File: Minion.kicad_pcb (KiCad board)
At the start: 0 parts

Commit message: finished most of pcb, added 3d models
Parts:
- added BT1: Battery, Connector_JST:JST_PH_S2B-PH-K_1x02_P2.00mm_Horizontal, F.Cu at (219.1, 155.0)
- added C1: 10uF, Capacitor_SMD:C_0805_2012Metric, F.Cu at (210.0, 157.0)
- added C10: 0.1uF, Capacitor_SMD:C_0805_2012Metric, F.Cu at (189.5, 122.5)
- added C11: 10uF, Capacitor_SMD:C_0805_2012Metric, F.Cu at (202.5, 153.5)
- added C2: 1uF, Capacitor_SMD:C_0805_2012Metric, F.Cu at (184.5, 124.5)
- added C3: 0.1uF, Capacitor_SMD:C_0805_2012Metric, F.Cu at (170.0, 135.5)
- added C4: 10uF, Capacitor_SMD:C_0805_2012Metric, F.Cu at (170.0, 139.0)
- added C5: 10uF, Capacitor_SMD:C_0805_2012Metric, F.Cu at (202.0, 125.5)
- added C6: 0.1uF, Capacitor_SMD:C_0805_2012Metric, F.Cu at (199.5, 125.5)
- added C7: 10uF, Capacitor_SMD:C_0805_2012Metric, F.Cu at (206.9, 115.0)
- added C8: 0.1uF, Capacitor_SMD:C_0805_2012Metric, F.Cu at (210.0, 118.0)
- added C9: 0.1uF, Capacitor_SMD:C_0805_2012Metric, F.Cu at (198.0, 101.5)
- added D1: PWRLED, LED_SMD:LED_0805_2012Metric, F.Cu at (210.5, 114.0)
- added D2: WS2812B, LED_SMD:LED_WS2812B_PLCC4_5.0x5.0mm_P3.2mm, B.Cu at (191.6, 135.3)
- added D3: WS2812B, LED_SMD:LED_WS2812B_PLCC4_5.0x5.0mm_P3.2mm, B.Cu at (201.1, 135.3)
- added D4: WS2812B, LED_SMD:LED_WS2812B_PLCC4_5.0x5.0mm_P3.2mm, B.Cu at (201.1, 127.5)
- added D5: WS2812B, LED_SMD:LED_WS2812B_PLCC4_5.0x5.0mm_P3.2mm, B.Cu at (191.5, 127.7)
- added D6: S-LMBR340FT1G, Diode_SMD:D_0805_2012Metric, F.Cu at (195.5, 108.0)
- added D8: Orange, LED_SMD:LED_0805_2012Metric, F.Cu at (212.0, 150.0)
- added D9: MBR0540, Diode_SMD:D_SOD-123, F.Cu at (206.5, 150.5)
- added DISPLAY_SSD1351: Conn_01x07_Socket, Connector_PinHeader_2.54mm:SSD_1351, F.Cu at (175.0, 123.3)
- added J1: USB_C_Receptacle_USB2.0_16P, Connector_USB:USB_C_Receptacle_HCTL_HC-TYPE-C-16P-01A, F.Cu at (204.5, 103.0)
- added J2: USB_A, Connector_USB:USB_A_Molex_105057_Vertical, F.Cu at (171.0, 156.5)
- added J3: Micro_SD_Card, Connector_Card:microSD_HC_Molex_47219-2001, F.Cu at (190.6, 151.0)
- added Q1: AO3401A, Package_TO_SOT_SMD:SOT-23, F.Cu at (206.4, 155.6)
- added R10: 1k, Resistor_SMD:R_0805_2012Metric, F.Cu at (203.9, 113.0)
- added R11: 4.7k, Resistor_SMD:R_0805_2012Metric, F.Cu at (211.5, 152.9)
- added R12: 4.7k, Resistor_SMD:R_0805_2012Metric, F.Cu at (215.0, 152.5)
- added R13: 4.7k, Resistor_SMD:R_0805_2012Metric, F.Cu at (178.5, 131.0)
- added R14: 4.7k, Resistor_SMD:R_0805_2012Metric, F.Cu at (178.5, 133.5)
- added R3: 5.1k, Resistor_SMD:R_0805_2012Metric, F.Cu at (207.0, 109.0)
- added R4: 5.1k, Resistor_SMD:R_0805_2012Metric, F.Cu at (199.4, 109.5)
- added R5: 10k, Resistor_SMD:R_0805_2012Metric, F.Cu at (198.0, 105.0)
- added R6: 10k, Resistor_SMD:R_0805_2012Metric, F.Cu at (184.5, 121.0)
- added R7: 2.7k, Resistor_SMD:R_0805_2012Metric, F.Cu at (186.5, 130.0)
- added R8: 4.7k, Resistor_SMD:R_0805_2012Metric, F.Cu at (210.5, 122.5)
- added R9: 4.7k, Resistor_SMD:R_0805_2012Metric, F.Cu at (210.5, 125.5)
- added SW1: SW_Push, Button_Switch_SMD:SW_Push_1P1T_NO_6x6mm_H9.5mm, F.Cu at (221.5, 123.5)
- added SW2: SW_Push, Button_Switch_SMD:SW_Push_1P1T_NO_6x6mm_H9.5mm, F.Cu at (221.5, 134.0)
- added SW3: SW_Push, Button_Switch_SMD:SW_Push_1P1T_NO_6x6mm_H9.5mm, F.Cu at (221.5, 144.5)
- added SW4: RotaryEncoder_Switch, Rotary_Encoder:RotaryEncoder_Bourns_Vertical_PEC12R-3x17F-Nxxxx, F.Cu at (216.0, 113.2)
- added SW5: SW_Push, Button_Switch_SMD:SW_Push_1P1T_NO_CK_KMR2, F.Cu at (194.5, 103.0)
- added SW6: SW_Push, Button_Switch_SMD:SW_Push_1P1T_NO_CK_KMR2, F.Cu at (178.8, 124.5)
- added U1: ESP32-S3-WROOM-1, RF_Module:ESP32-S3-WROOM-1, F.Cu at (179.0, 109.9)
- added U2: AMS1117-3.3, Package_TO_SOT_SMD:SOT-223-3_TabPin2, F.Cu at (204.0, 120.0)
- added U3: FE1.1s, Package_SO:SSOP-28_3.9x9.9mm_P0.635mm, F.Cu at (184.1, 137.1)
- added U4: ADXL343, Package_LGA:LGA-14_3x5mm_P0.8mm_LayoutBorder1x6y, F.Cu at (209.0, 129.5)
- added U5: CH376T, Package_SO:SSOP-20_5.3x7.2mm_P0.65mm, F.Cu at (205.0, 144.0)
- added U6: MCP73831-2-MC, Package_DFN_QFN:DFN-8-1EP_3x2mm_P0.5mm_EP1.7x1.4mm, F.Cu at (214.6, 156.7)
- added Y1: 12MHz, Crystal:Crystal_SMD_5032-2Pin_5.0x3.2mm, F.Cu at (196.5, 140.5)
- added Y2: 12MHz, Crystal:Crystal_SMD_5032-2Pin_5.0x3.2mm, F.Cu at (209.0, 136.5)
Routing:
- net GND: track 0.00 -> 160.8 mm, vias 0 -> 32
- net +3V3: track 0.00 -> 139.0 mm, vias 0 -> 8
- net +5V: track 0.00 -> 103.3 mm, vias 0 -> 7
- net VUSB: track 0.00 -> 97.5 mm, vias 0 -> 4
- net IO14: track 0.00 -> 59.2 mm, vias 0 -> 1
- net IO6: track 0.00 -> 53.2 mm, vias 0 -> 2
- net IO13: track 0.00 -> 52.3 mm, vias 0 -> 4
- net IO12: track 0.00 -> 49.0 mm, vias 0 -> 4
- net IO5: track 0.00 -> 47.0 mm, vias 0 -> 2
- net IO11: track 0.00 -> 46.2 mm, vias 0 -> 1
- net IO4: track 0.00 -> 43.7 mm, vias 0 -> 2
- net IO10: track 0.00 -> 41.1 mm, vias 0 -> 1
- net DUP: track 0.00 -> 40.5 mm, vias 0 -> 2
- net DUN: track 0.00 -> 40.4 mm, vias 0 -> 2
- net IO8/SDA: track 0.00 -> 31.4 mm, vias 0 -> 6
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- added copper zone on B.Cu, net GND
- added copper zone on F.Cu, net GND
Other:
- board outline added: 60 x 60 mm
- copper layers 0 -> 2

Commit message: finished pcb and updated journal
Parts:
- removed U4: ADXL343, Package_LGA:LGA-14_3x5mm_P0.8mm_LayoutBorder1x6y
- added C12: 1uF, Capacitor_SMD:C_0805_2012Metric, F.Cu at (184.5, 147.5)
- added C13: 1uF, Capacitor_SMD:C_0805_2012Metric, F.Cu at (195.2, 146.8)
- added C14: 1uF, Capacitor_SMD:C_0805_2012Metric, F.Cu at (195.2, 144.8)
- added C15: 1uF, Capacitor_SMD:C_0805_2012Metric, F.Cu at (195.2, 148.8)
- added C16: 1uF, Capacitor_SMD:C_0805_2012Metric, F.Cu at (178.9, 152.8)
- added C17: 1uF, Capacitor_SMD:C_0805_2012Metric, F.Cu at (188.8, 151.8)
- added H1: MountingHole, MountingHole:MountingHole_2.2mm_M2, F.Cu at (169.2, 138.0)
- added H2: MountingHole, MountingHole:MountingHole_2.2mm_M2, F.Cu at (215.5, 124.5)
- added J4: PJ-320D-A, PJ-320D-A:HRO_PJ-320D-A, B.Cu at (180.8, 154.5)
- added R1: 1k, Resistor_SMD:R_0805_2012Metric, F.Cu at (183.8, 151.8)
- added R2: 1k, Resistor_SMD:R_0805_2012Metric, F.Cu at (180.8, 155.2)
- added U7: PCM5102A, Package_SO:TSSOP-20_4.4x6.5mm_P0.65mm, F.Cu at (189.8, 146.4)
- J2: footprint Connector_USB:USB_A_Molex_105057_Vertical -> Connector_USB:USB_A_Molex_67643_Horizontal; moved to B.Cu
- J3: value Micro_SD_Card -> 473092651; footprint Connector_Card:microSD_HC_Molex_47219-2001 -> 473092651:CONN12_47309-2651_MOL
- SW4: value RotaryEncoder_Switch -> RotaryEncoder
- moved C4 18.8 mm to (174.5, 120.8)
- moved C3 18.1 mm to (180.5, 120.8)
- moved Y2 7.59 mm to (211.2, 143.8), turned to -90 degrees
- moved J3 4.76 mm to (191.0, 155.8)
- moved D6 4.50 mm to (200.0, 108.0), turned to 90 degrees
- moved J2 3.74 mm to (172.9, 153.2), turned to 90 degrees
- moved R4 3.43 mm to (202.5, 108.0), turned to 90 degrees
- moved R7 3.35 mm to (189.5, 131.5), turned to 0 degrees
- moved R14 3.04 mm to (178.0, 130.5)
- moved SW1 3.00 mm to (221.5, 120.5)
- moved SW2 3.00 mm to (221.5, 131.0)
- moved SW3 3.00 mm to (221.5, 141.5)
- moved R13 2.55 mm to (178.0, 128.5)
- moved J1 1.75 mm to (204.5, 101.2)
- moved C6 0.25 mm to (199.8, 125.5), turned to -90 degrees
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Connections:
- U1 pad 10: unconnected-(U1-IO17-Pad10) -> BCK
- U1 pad 23: unconnected-(U1-IO21-Pad23) -> DIN_Audio
- U1 pad 9: unconnected-(U1-IO16-Pad9) -> LRCK
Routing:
- net GND: track 160.8 -> 69.0 mm, vias 32 -> 26
- net DIN_Audio: track 0.00 -> 68.9 mm, vias 0 -> 4
- net BCK: track 0.00 -> 58.1 mm, vias 0 -> 2
- net LRCK: track 0.00 -> 34.2 mm, vias 0 -> 2
- net VUSB: track 97.5 -> 72.4 mm, vias 4 -> 3
- net +5V: track 103.3 -> 122.6 mm, vias 7 -> 5
- net Net-(U7-OUTL): track 0.00 -> 14.5 mm
- net IO14: track 59.2 -> 45.8 mm, vias 1 -> 3
- net RIGHT: track 0.00 -> 7.67 mm
- net Net-(U5-XO): track 17.5 -> 9.88 mm
- net Net-(U7-LDOO): track 0.00 -> 7.38 mm
- net SCK: track 15.3 -> 22.3 mm
- net Net-(U7-CAPM): track 0.00 -> 6.96 mm
- net SDO: track 13.9 -> 20.7 mm
- net Net-(U3-XOUT): track 19.1 -> 12.8 mm, vias 2 -> 0
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
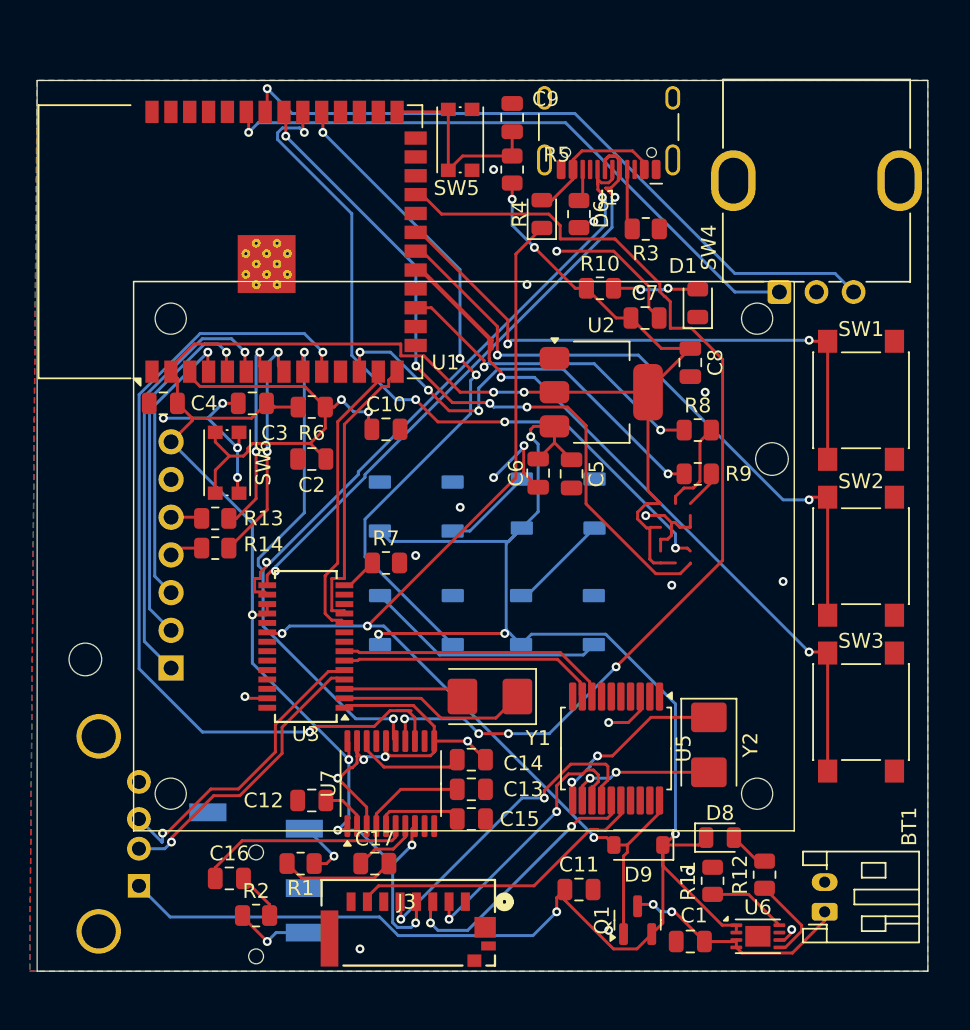
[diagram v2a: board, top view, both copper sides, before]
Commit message: Updated from feedback
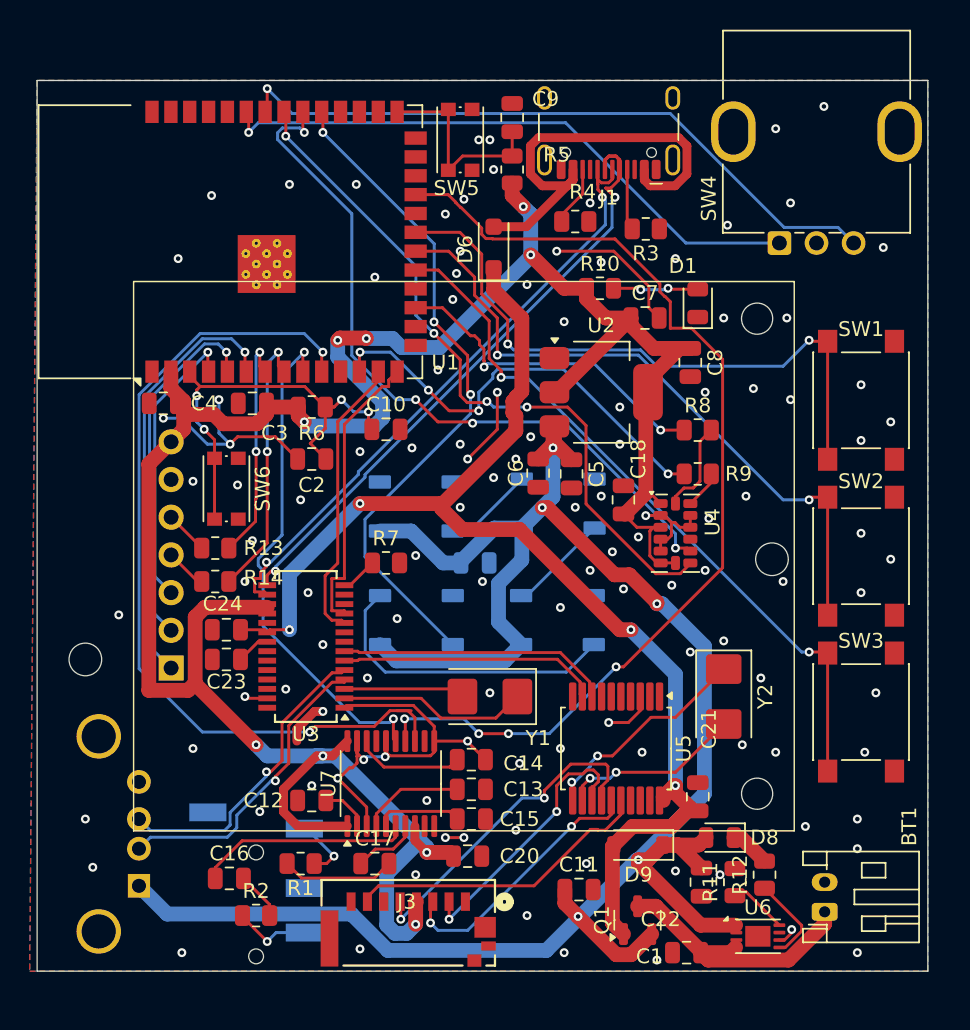
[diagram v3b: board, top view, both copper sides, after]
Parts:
- added C18: 0.1uF, Capacitor_SMD:C_0805_2012Metric, F.Cu at (205.5, 127.2)
- added C19: 4.7uF, Capacitor_SMD:C_0805_2012Metric, B.Cu at (195.5, 131.5)
- added C20: 0.1uF, Capacitor_SMD:C_0805_2012Metric, F.Cu at (195.0, 151.2)
- added C21: 0.1uF, Capacitor_SMD:C_0805_2012Metric, F.Cu at (210.5, 147.2)
- added C22: 4.7uF, Capacitor_SMD:C_0805_2012Metric, F.Cu at (210.8, 153.0)
- added C23: 10uF, Capacitor_SMD:C_0805_2012Metric, F.Cu at (178.8, 138.0)
- added C24: 0.1uF, Capacitor_SMD:C_0805_2012Metric, F.Cu at (178.8, 136.0)
- added U4: ADXL343, Package_LGA:LGA-14_3x5mm_P0.8mm_LayoutBorder1x6y, F.Cu at (209.0, 129.5)
- C1: value 10uF -> 4.7uF
- D6: footprint Diode_SMD:D_0805_2012Metric -> Diode_SMD:D_SOD-123F
- R11: value 4.7k -> 2k
- R12: value 4.7k -> 0.47k
- moved H2 6.75 mm to (215.5, 131.2)
- moved D6 3.95 mm to (196.8, 110.2)
- moved Y2 3.40 mm to (212.2, 140.5)
- moved SW4 3.30 mm to (216.0, 110.0)
- moved R14 2.25 mm to (178.0, 132.8)
- moved R13 2.00 mm to (178.0, 130.5)
- moved SW6 1.75 mm to (178.8, 126.5)
- moved R11 1.50 mm to (213.0, 153.0)
- moved C1 0.79 mm to (209.8, 157.8)
- moved R4 0.56 mm to (202.2, 108.5), turned to 180 degrees
- turned D8 to 180 degrees
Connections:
- D8 pad 1: +5V -> Net-(D8-K)
- D8 pad 2: Net-(D8-A) -> +5V
- R12 pad 2: Net-(D8-A) -> Net-(D8-K)
- U3 pad 21: unconnected-(U3-VD33_O-Pad21) -> Net-(U3-VD33_O)
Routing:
- net +3V3: track 136.9 -> 171.5 mm
- net Net-(D6-A): track 9.83 -> 29.6 mm
- net +5V: track 122.6 -> 137.8 mm
- net VUSB: track 72.4 -> 82.6 mm, vias 3 -> 4
- net IO6: track 55.4 -> 48.5 mm
- net GND: track 69.0 -> 73.9 mm, vias 26 -> 117
- net Net-(D2-DOUT): track 16.3 -> 20.9 mm
- net IO4: track 39.9 -> 42.7 mm
- net Net-(D8-K): track 0.00 -> 2.72 mm
- net Net-(D8-A): track 2.72 -> 0.00 mm
- net VBAT: track 15.9 -> 18.5 mm, vias 2 -> 0
- net Net-(U5-XI): track 12.4 -> 14.8 mm
- net Net-(U5-XO): track 9.88 -> 12.2 mm
- net Net-(U3-VD33_O): track 0.00 -> 2.29 mm
- net SLK: track 16.1 -> 18.3 mm
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
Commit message: Finished PCB!
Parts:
- removed C19: 4.7uF, Capacitor_SMD:C_0805_2012Metric
- removed D2, D3, D4, D5: WS2812B, LED_SMD:LED_WS2812B_PLCC4_5.0x5.0mm_P3.2mm
- removed D6: S-LMBR340FT1G, Diode_SMD:D_SOD-123F
- removed DISPLAY_SSD1351: Conn_01x07_Socket, Connector_PinHeader_2.54mm:SSD_1351
- removed U5: CH376T, Package_SO:SSOP-20_5.3x7.2mm_P0.65mm
- removed Y1, Y2: 12MHz, Crystal:Crystal_SMD_5032-2Pin_5.0x3.2mm
- added C26: 0.1uF, Capacitor_SMD:C_0805_2012Metric, F.Cu at (168.5, 150.6)
- added C27: 4.7uF, Capacitor_SMD:C_0805_2012Metric, F.Cu at (168.5, 147.1)
- added C28: 4.7uF, Capacitor_SMD:C_0805_2012Metric, F.Cu at (183.9, 141.2)
- added C29: 0.1uF, Capacitor_SMD:C_0805_2012Metric, F.Cu at (181.9, 141.2)
- added C30: 0.1uF, Capacitor_SMD:C_0805_2012Metric, F.Cu at (168.5, 144.1)
- added C31: 0.1uF, Capacitor_SMD:C_0805_2012Metric, F.Cu at (187.9, 141.9)
- added C32: 18pF, Capacitor_SMD:C_0402_1005Metric, F.Cu at (190.7, 144.9)
- added C33: 18pF, Capacitor_SMD:C_0402_1005Metric, F.Cu at (190.6, 146.9)
- added J5: Conn_01x07_Socket, Connector_PinHeader_2.54mm:SSD_1351, F.Cu at (175.0, 122.8)
- added R15: 10k, Resistor_SMD:R_0805_2012Metric, F.Cu at (167.5, 141.3)
- added R16: 10k, Resistor_SMD:R_0805_2012Metric, F.Cu at (169.5, 141.3)
- added R17: 100k, Resistor_SMD:R_0805_2012Metric, F.Cu at (186.5, 148.8)
- added R18: 100k, Resistor_SMD:R_0805_2012Metric, F.Cu at (183.1, 149.0)
- added R19: 1M, Resistor_SMD:R_0805_2012Metric, F.Cu at (181.6, 146.3)
- added R20: 10k, Resistor_SMD:R_0805_2012Metric, F.Cu at (179.3, 153.6)
- added R21: 100k, Resistor_SMD:R_0805_2012Metric, F.Cu at (178.3, 130.6)
- added R22: 12k, Resistor_SMD:R_0805_2012Metric, F.Cu at (185.9, 141.5)
- added U8: USB2641I-HZH-02, USB2641:QFN48_7X7MC_MCH, F.Cu at (175.9, 147.7)
- added Y3: 24MHz, Crystal:Crystal_SMD_5032-2Pin_5.0x3.2mm, F.Cu at (185.8, 145.8)
- BT1: moved to B.Cu
- C10: value 0.1uF -> 10uF
- C2: value 1uF -> 10uF
- J4: moved to F.Cu
- R13, R14, R8, R9: value 4.7k -> 4k7
- R3, R4: value 5.1k -> 5k1
- R7: value 2.7k -> 10k
- U2: value AMS1117-3.3 -> AP2112K-3.3; footprint Package_TO_SOT_SMD:SOT-223-3_TabPin2 -> Package_TO_SOT_SMD:SOT-23-5
- U3: value FE1.1s -> AP2112K-3.3; footprint Package_SO:SSOP-28_3.9x9.9mm_P0.635mm -> Package_TO_SOT_SMD:SOT-23-5
- moved J1 56.7 mm to (186.1, 154.9), turned to 0 degrees
- moved R3 43.4 mm to (189.9, 148.9)
- moved R4 41.5 mm to (193.4, 149.0), turned to -90 degrees
- moved J4 40.4 mm to (221.2, 153.8)
- moved R1 37.0 mm to (220.2, 145.6), turned to 0 degrees
- moved C16 35.4 mm to (213.3, 144.3)
- moved R2 34.9 mm to (215.1, 149.3), turned to 90 degrees
- moved C21 33.9 mm to (178.0, 137.4)
- moved J2 31.3 mm to (204.0, 150.5), turned to 180 degrees
- moved C17 29.0 mm to (216.7, 144.2)
- moved C7 27.6 mm to (199.8, 141.6)
- moved H1 26.6 mm to (194.7, 130.5)
- moved U2 25.2 mm to (200.7, 145.0), turned to 90 degrees
- moved C20 25.1 mm to (213.4, 134.2)
- moved C12 24.3 mm to (205.8, 135.9)
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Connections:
- net BCK renamed BCK_Audio
- net IO10 renamed ROTARY_A
- net IO11 renamed ROTARY_B
- net IO12 renamed ADXL_INT1
- net IO13 renamed ADXL_INT2
- net IO4 renamed BUTTON_1
- net IO5 renamed BUTTON_2
- net IO6 renamed BUTTON_3
- net LRCK renamed LRCK_Audio
- C10 pad 1: CHIP_PU -> ESP_EN
- C2 pad 1: GND -> VUSB
- C2 pad 2: CHIP_PU -> GND
- C23 pad 1: GND -> VUSB3V3
- C23 pad 2: Net-(U3-VD33_O) -> GND
- C24 pad 1: VUSB -> VUSB3V3
- J1 pad A4: Net-(D6-A) -> VUSB
- J1 pad A9: Net-(D6-A) -> VUSB
- J1 pad B4: Net-(D6-A) -> VUSB
- J1 pad B9: Net-(D6-A) -> VUSB
- J2 pad 1: +5V -> VUSB
- J2 pad 2: D4N -> D2N
- J2 pad 3: D4P -> D2P
- J3 pad 1: unconnected-(J3-Pad1) -> SD_D2
- J3 pad 2: SCS -> SD_D3
- J3 pad 3: SDI -> SD_CMD
- J3 pad 4: +3V3 -> VUSB3V3
- J3 pad 5: SCK -> SD_CLK
- J3 pad 7: SDO -> SD_D0
- J3 pad 8: unconnected-(J3-Pad8) -> SD_D1
- J4 pad 2: Net-(J4-Pad2) -> RIGHT
- J4 pad 4: Net-(J4-Pad4) -> LEFT
- R1 pad 1: Net-(J4-Pad2) -> RIGHT
- R1 pad 2: RIGHT -> GND
- R13 pad 1: Net-(DISPLAY_SSD1351-Pin_5) -> DIN_Display
- R13 pad 2: DIN -> +3V3
- R14 pad 1: Net-(DISPLAY_SSD1351-Pin_4) -> SLK_Display
- R14 pad 2: SLK -> +3V3
- R2 pad 1: Net-(J4-Pad4) -> LEFT
- R2 pad 2: LEFT -> GND
- R6 pad 2: CHIP_PU -> Net-(R21-Pad1)
- R7 pad 1: Net-(U3-REXT) -> VUSB
- R8 pad 1: IO9/SCL -> +3V3
- R8 pad 2: Net-(U4-SCL/SCLK) -> ADXL_SCL
- R9 pad 1: IO8/SDA -> +3V3
- R9 pad 2: Net-(U4-SDA/SDI/SDIO) -> ADXL_SDA
- SW6 pad 2: CHIP_PU -> Net-(R21-Pad1)
- U1 pad 12: IO8/SDA -> ADXL_SDA
- U1 pad 17: IO9/SCL -> ADXL_SCL
- U1 pad 3: CHIP_PU -> ESP_EN
- U1 pad 31: IO14 -> Neopixels
- U1 pad 4: CS -> CS_Display
- U1 pad 5: DC -> DC_Display
- U1 pad 6: RST -> RST_Display
- U1 pad 7: DIN -> DIN_Display
- U1 pad 8: SLK -> SLK_Display
- U2 pad 1: GND -> +5V
- U2 pad 2: +3V3 -> GND
- U3 pad 1: GND -> VUSB
- U3 pad 2: Net-(U3-XOUT) -> GND
- U3 pad 3: Net-(U3-XIN) -> VUSB
- U3 pad 4: D4N -> unconnected-(U3-NC-Pad4)
- U3 pad 5: D4P -> VUSB3V3
- U4 pad 13: Net-(U4-SDA/SDI/SDIO) -> ADXL_SDA
- U4 pad 14: Net-(U4-SCL/SCLK) -> ADXL_SCL
- U7 pad 12: unconnected-(U7-SCK-Pad12) -> GND
- U7 pad 17: GND -> +3V3
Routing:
- net +3V3: track 171.5 -> 65.2 mm, vias 9 -> 16
- net +5V: track 137.8 -> 40.1 mm, vias 5 -> 0
- net GND: track 73.9 -> 1.77 mm, vias 117 -> 63
- net VUSB: track 82.6 -> 34.0 mm
- net IO14: track 45.4 -> 0.00 mm, vias 3 -> 0
- net VUSB3V3: track 0.00 -> 39.1 mm, vias 0 -> 7
- net D2N: track 0.00 -> 36.7 mm
- net D2P: track 0.00 -> 36.1 mm
- net IO8/SDA: track 29.8 -> 0.00 mm, vias 4 -> 0
- net Net-(D6-A): track 29.6 -> 0.00 mm
- net RST: track 29.1 -> 0.00 mm, vias 1 -> 0
- net CHIP_PU: track 28.9 -> 0.00 mm, vias 4 -> 0
- net DUN: track 43.6 -> 15.5 mm, vias 2 -> 0
- net DUP: track 42.3 -> 16.3 mm, vias 2 -> 0
- net ADXL_SDA: track 0.00 -> 25.8 mm, vias 0 -> 2
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- added copper zone on In2.Cu, net +3V3
- added copper zone on In1.Cu, net GND
- added copper zone on In2.Cu, net VUSB
- added copper zone on In2.Cu, net VUSB3V3
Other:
- copper layers 2 -> 4
- board text added: "-+"
